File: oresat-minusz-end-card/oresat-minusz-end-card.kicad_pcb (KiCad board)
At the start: 2 copper layers, 99 x 95.3 mm, 72 parts, among them J1 TFM-110-01-L-D-RA, J2 U.FL, J3 M55-7101242R, J4 M55-7101242R, J5 M55-7101242R, J6 M55-7101242R, J7 U.FL, J8 3220-10-0100-00, J9 U.FL, U2 TPS63070, U3 TCAN330GDCNT, U4 STM32F042K6T7, X2 ECS-160-10-36Q-ES-TR

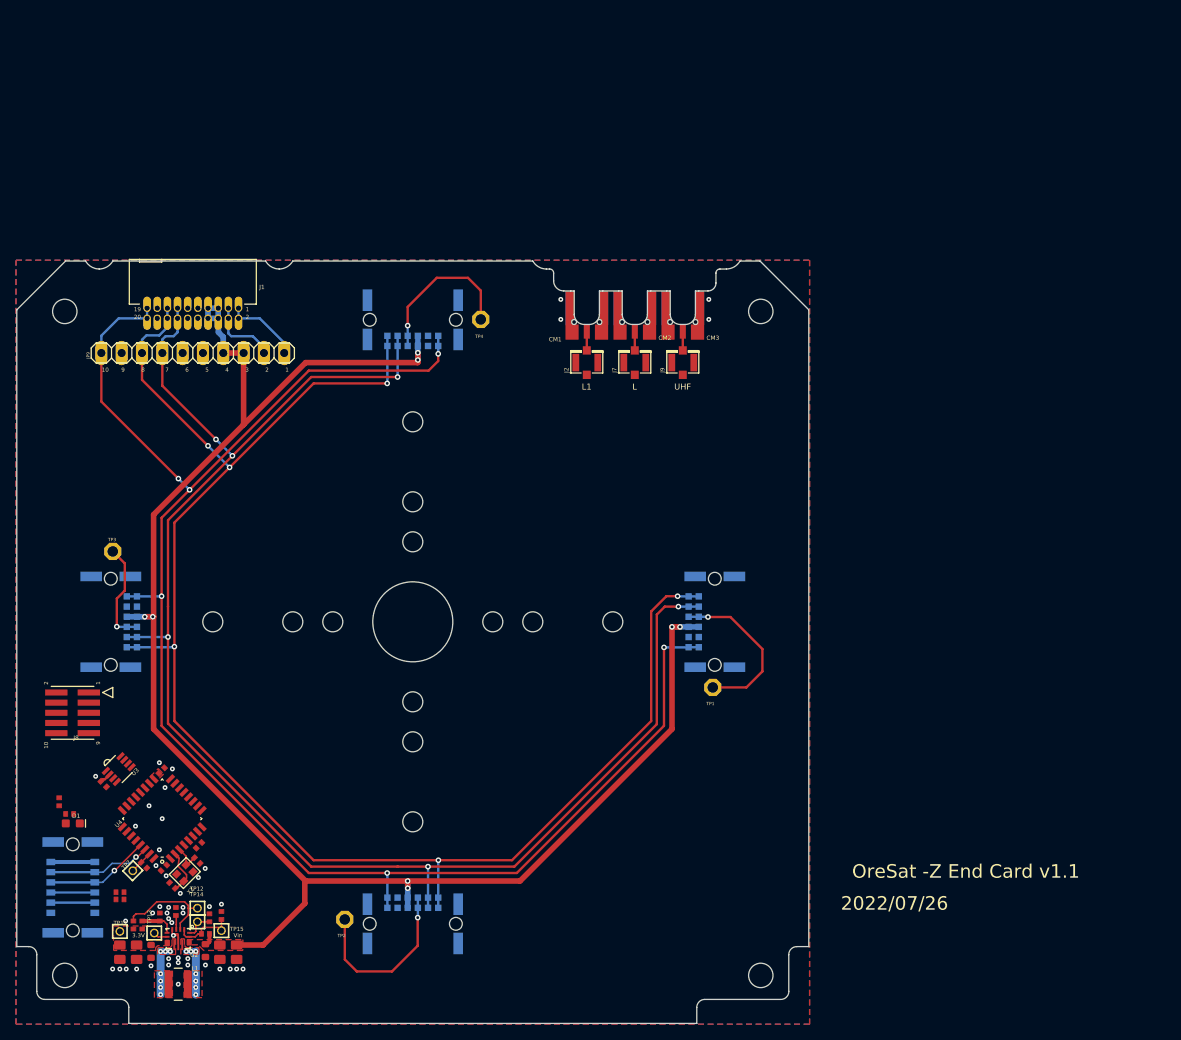
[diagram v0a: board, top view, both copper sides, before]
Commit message: Fixed some errors on the ancient -z end card
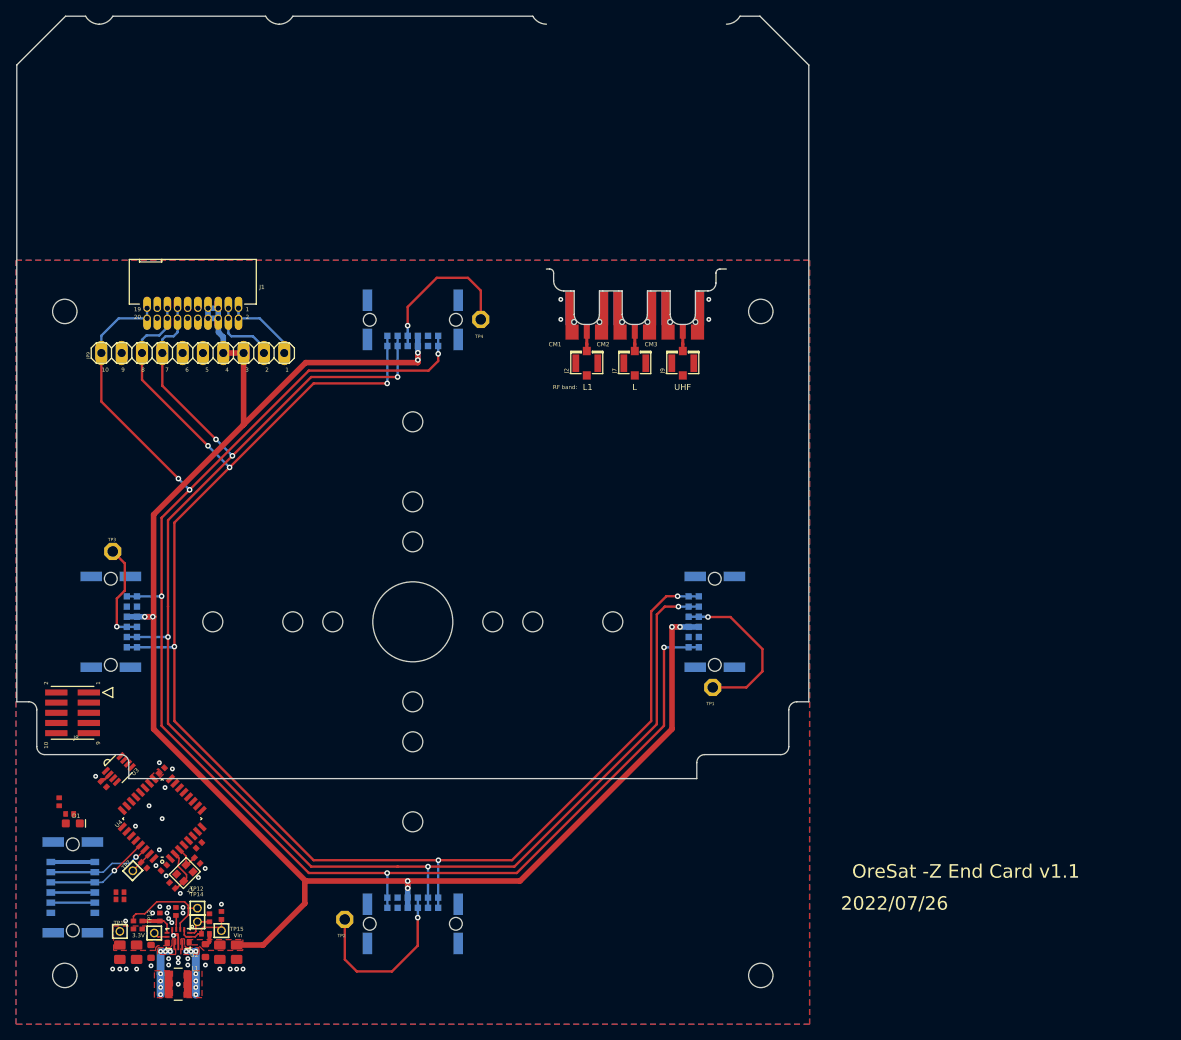
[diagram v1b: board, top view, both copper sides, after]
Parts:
- C1, C12, C15, C18, C2, C8, C9: value CL05B104KO5NNNC -> (none)
- C13, C14: value CL05C200JB51PNC -> (none)
- CM1, CM2, CM3: footprint oresat-minusz-end-card:J-MOLEX-SMPM-073300-003X -> oresat-footprints:J-MOLEX-SMPM-073300-003X
- J1: value TFM-110-01-L-D-RA -> (none)
- J2, J7, J9: footprint oresat-minusz-end-card:U.FL -> oresat-footprints:J-U.FL
- J8: value 3220-10-0100-00 -> (none)
- L1: value XFL4020-152ME -> (none)
- R1, R10, R11, R2, R3, R4, R5, R6, R7, R8, R9: value RC1005F6653CS -> (none)
- U2: value TPS63070 -> (none)
- U3: value TCAN330GDCNT -> (none)
- U4: value STM32F042K6T7 -> (none)
- X2: value ECS-160-10-36Q-ES-TR -> (none)
- moved CARD0 30.6 mm to (99.0, 122.1)
- moved J2 0.08 mm to (170.3, 70.1)
- moved J7 0.08 mm to (176.3, 70.1)
- moved J9 0.08 mm to (182.3, 70.1)
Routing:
- net UHF-TURNSTILE: track 2.36 -> 0.29 mm
- net L1-TURNSTILE: track 2.36 -> 0.29 mm
- net L-TURNSTILE: track 2.36 -> 0.29 mm
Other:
- board text added: "RF band:"
